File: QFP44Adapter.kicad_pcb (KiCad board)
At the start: 2 copper layers, 57.4 x 21.8 mm, 3 parts, among them J1 Conn_01x22_Male, J2 Conn_01x22_Male, U1 QFP44

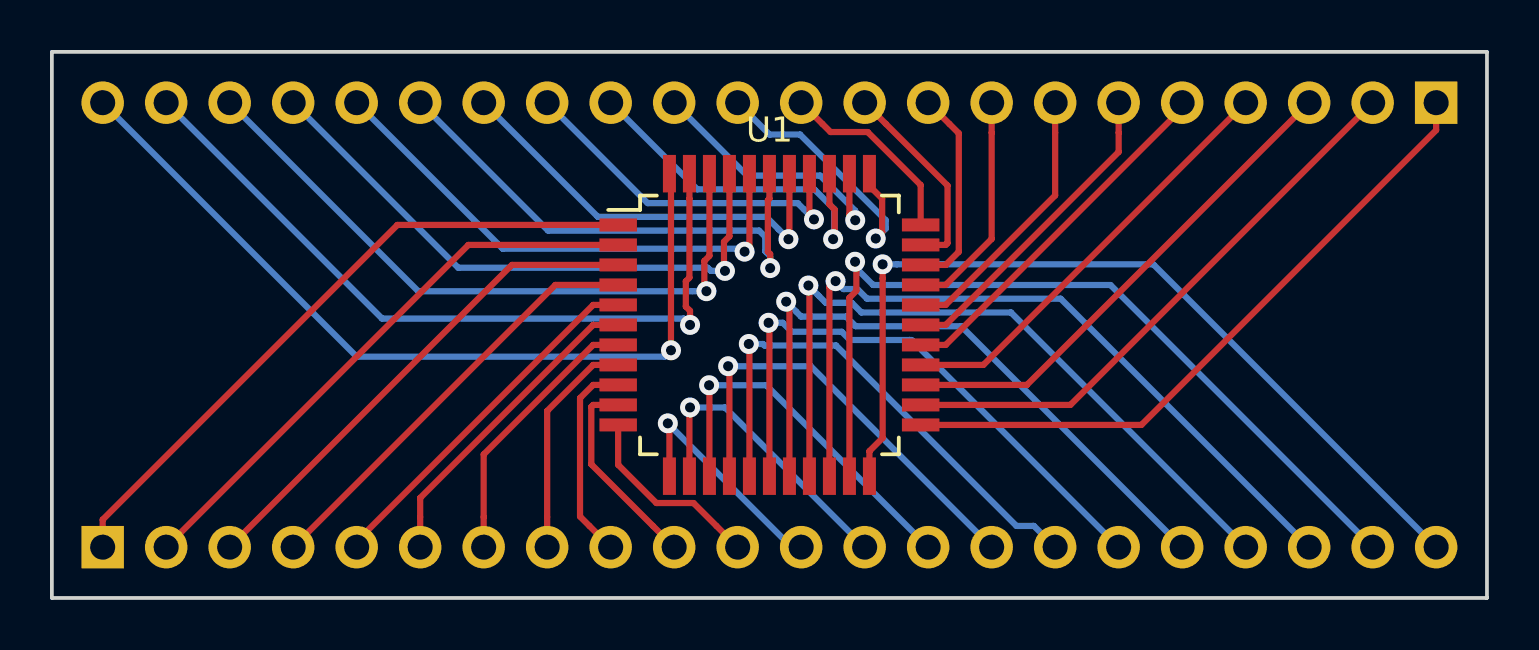
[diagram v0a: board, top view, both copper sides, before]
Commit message: Increase track width, add pin numbers to silk screen
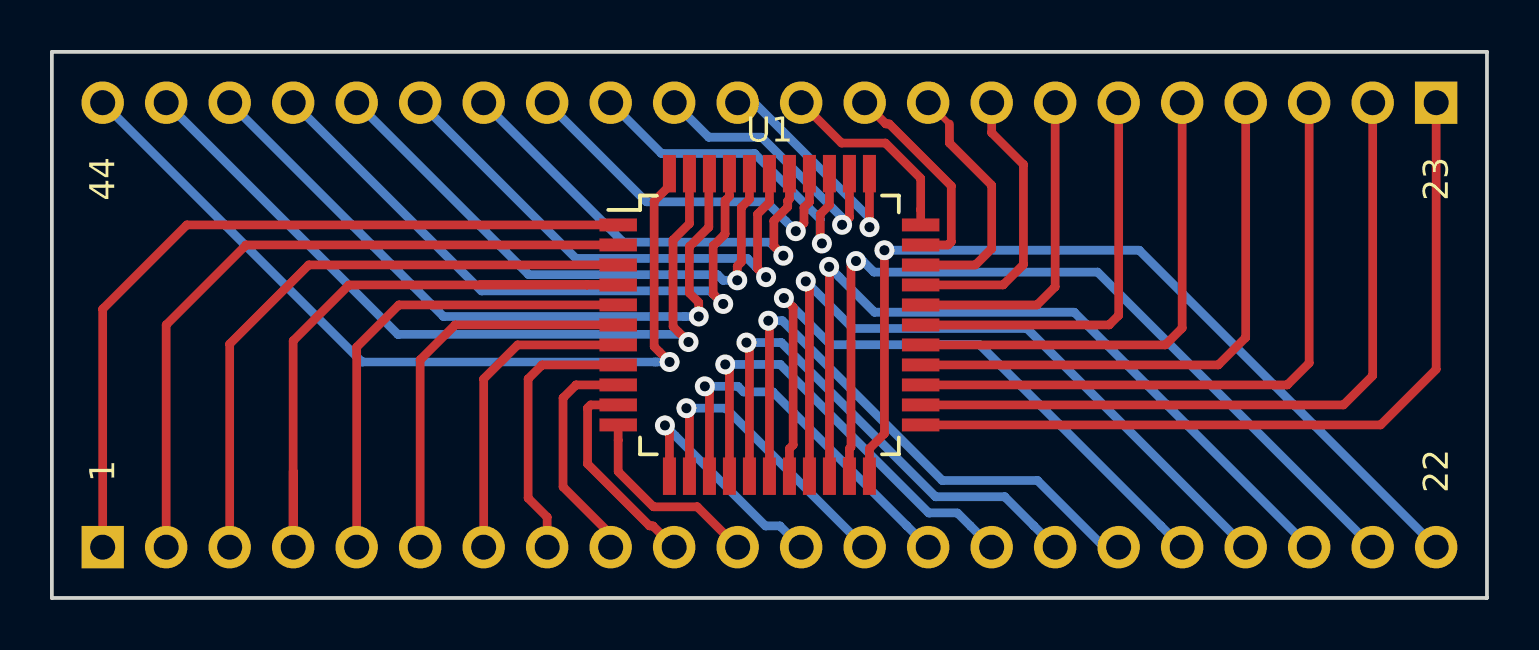
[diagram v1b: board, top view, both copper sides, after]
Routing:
- net 4: track 17.3 -> 32.1 mm
- net 24: track 23.1 -> 29.5 mm
- net 25: track 20.2 -> 26.3 mm
- net 23: track 26.6 -> 32.2 mm
- net 26: track 17.3 -> 22.9 mm
- net 2: track 23.1 -> 28.3 mm
- net 27: track 14.6 -> 19.8 mm
- net 1: track 26.6 -> 31.5 mm
- net 3: track 20.2 -> 25.0 mm
- net 5: track 14.6 -> 19.2 mm
- net 28: track 12.8 -> 16.6 mm
- net 6: track 12.8 -> 16.0 mm
- net 30: track 9.05 -> 11.4 mm
- net 29: track 10.9 -> 13.0 mm
- net 41: track 24.1 -> 26.2 mm
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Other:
- board text added: "1"
- board text added: "22"
- board text added: "23"
- board text added: "44"
